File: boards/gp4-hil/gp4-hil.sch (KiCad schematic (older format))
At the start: 8 parts

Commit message: Fixed a few pinout issues. Finished full-design pinout review.
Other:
- note removed: "Design review completed for PSU+Ethernet+FPGA support"
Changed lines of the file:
@@
 Wire Wire Line
 	4200 6750 3850 6750
-Text Notes 6350 6550 0    60   ~ 0
-Design review completed for PSU+Ethernet+FPGA support
 Text Label 2850 4150 0    60   ~ 0
 VPP_SHUNT_HI

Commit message: Minor refdes placement tweaks
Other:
- note added: "Bank plan\n* 14 (1V8): Boot flash, clock, Ethernet, JTAG\n* 15 (2V5): ADCs\n* 34 (variable): DUT bank 2\n* 35 (variable): DUT bank 1"
- note removed: "Bank plan\n* 14 (1V8): Boot flash, clock, Ethernet, JTAG\n* 15 (2V5): ADCs\n* 34 (variable): DUT bank 1\n* 35 (variable): DUT bank 2"
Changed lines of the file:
@@
 $EndSheet
 Text Notes 1250 12350 0    60   ~ 0
-Bank plan\n* 14 (1V8): Boot flash, clock, Ethernet, JTAG\n* 15 (2V5): ADCs\n* 34 (variable): DUT bank 1\n* 35 (variable): DUT bank 2
+Bank plan\n* 14 (1V8): Boot flash, clock, Ethernet, JTAG\n* 15 (2V5): ADCs\n* 34 (variable): DUT bank 2\n* 35 (variable): DUT bank 1
 Text Notes 1250 11600 0    60   ~ 0
 Possibly the most overkill dev board ever.\n* Target device has 26 LUTs and 12 FFs\n* Support FPGA has 63,400 LUTs and 126800 FFs (if you load the 100t)\n* Has an ADC, DAC, and digital I/O on every pin of the DUT, all bridged out to TCP sockets\n* TCP programming, simply netcat a bitstream to the board to flash the DUT

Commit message: Added pullups to default DUT_VDDx to 1V8 instead of floating
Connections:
- net 1V8: now also R172.1, R175.1
- net GND: no longer R172.1, R175.1

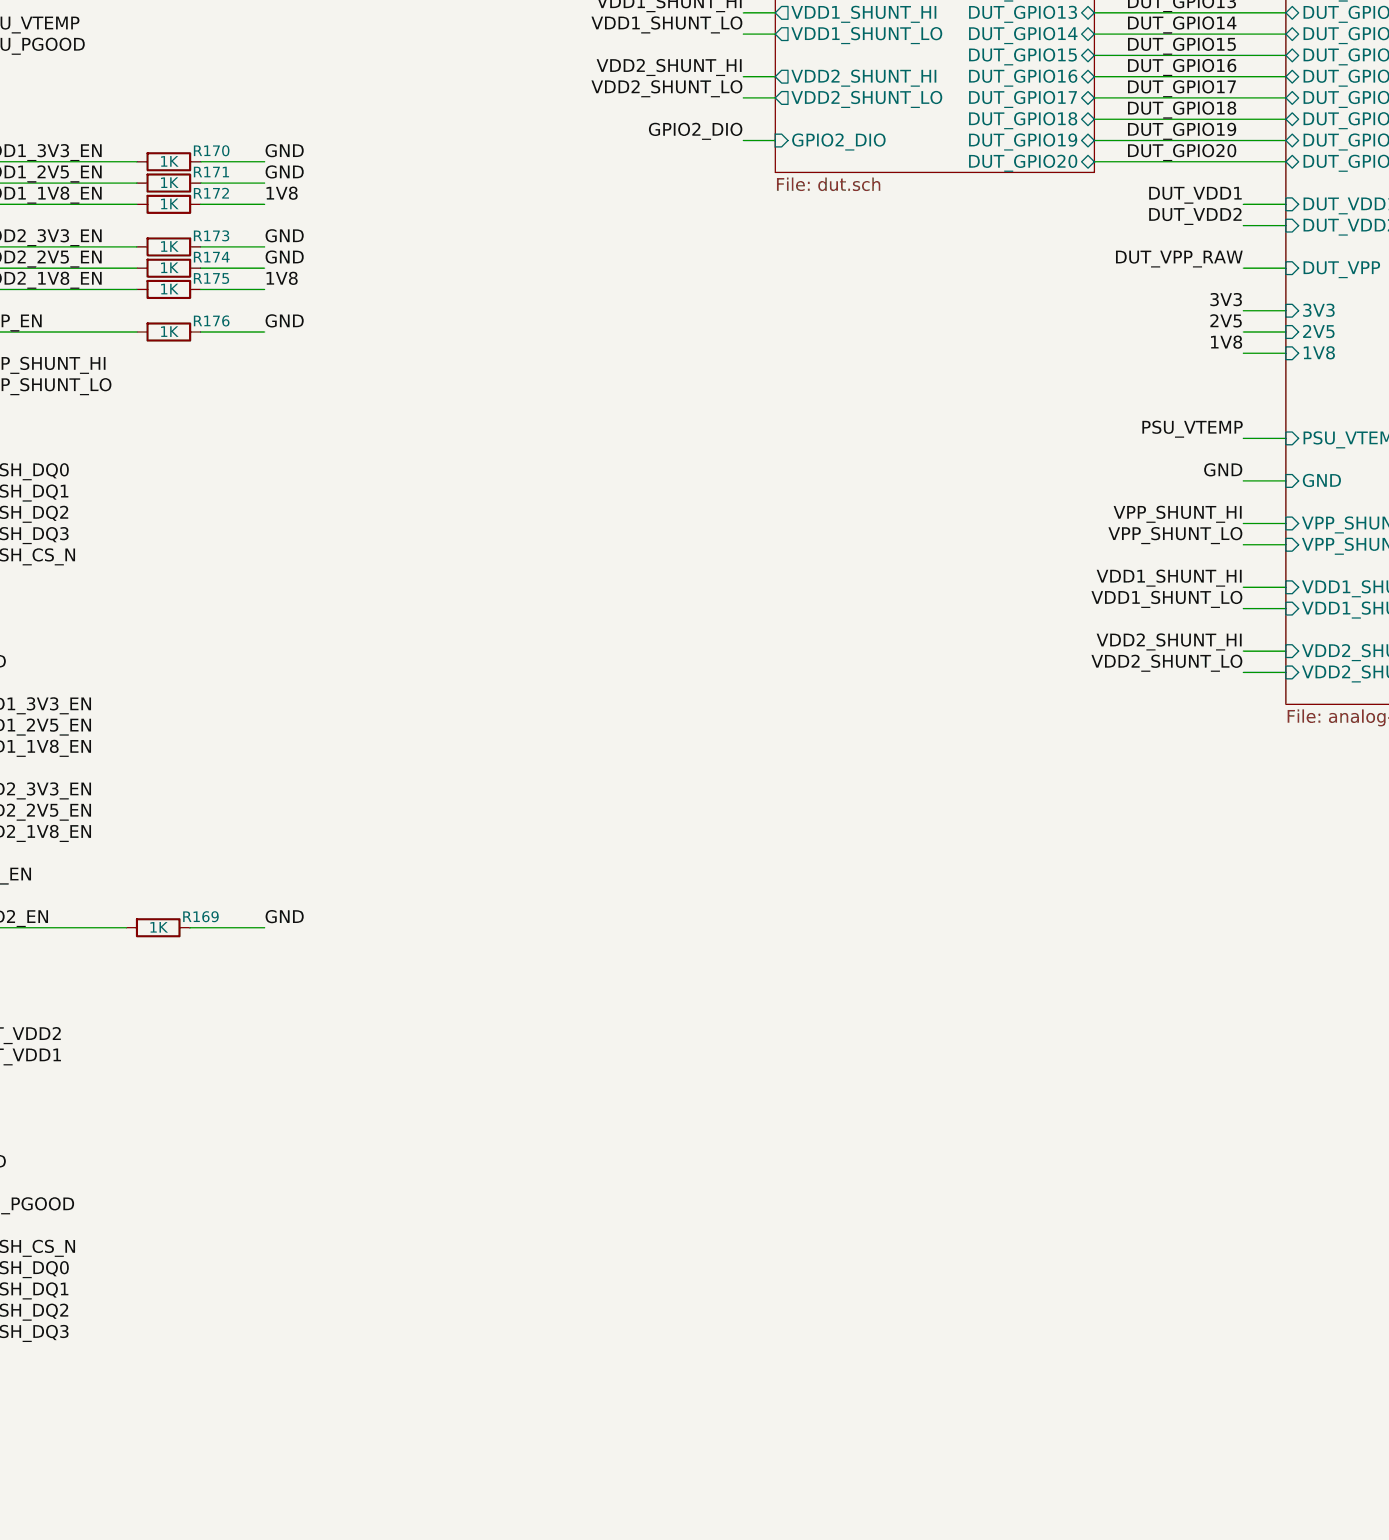
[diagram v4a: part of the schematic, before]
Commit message: Added jumpers to Vdd enable lines so they can be strapped high without FPGA involvement
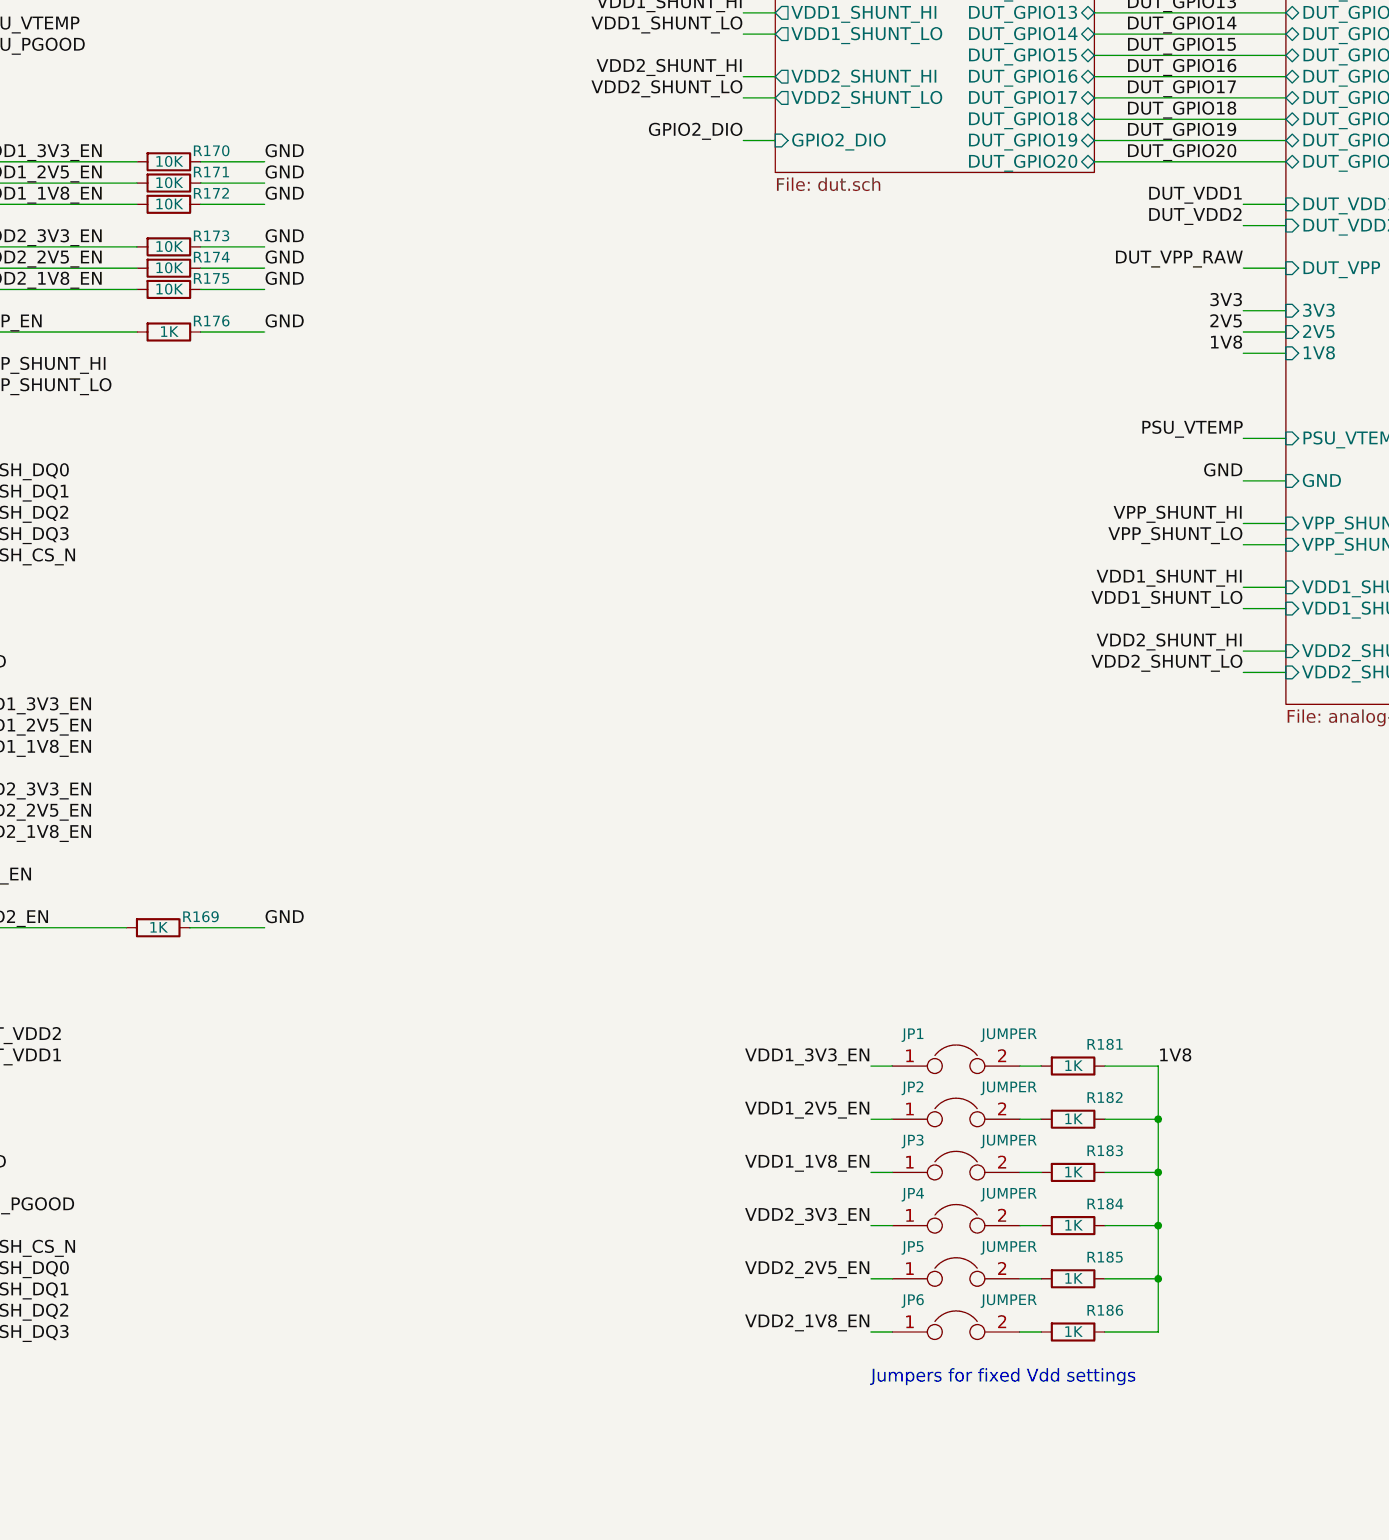
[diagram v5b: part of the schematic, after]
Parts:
- added JP1, JP2, JP3, JP4, JP5, JP6: JUMPER, symbol JUMPER
- added R181, R182, R183, R184, R185, R186: 1K, symbol R
- R170, R171, R172, R173, R174, R175: value 1K -> 10K
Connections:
- net 1V8: now also R181.1, R182.1, R183.1, R184.1, R185.1, R186.1; no longer R172.1, R175.1
- net GND: now also R172.1, R175.1
- net VDD1_1V8_EN: now also JP3.1
- net VDD1_2V5_EN: now also JP2.1
- net VDD1_3V3_EN: now also JP1.1
- net VDD2_1V8_EN: now also JP6.1
- net VDD2_2V5_EN: now also JP5.1
- net VDD2_3V3_EN: now also JP4.1
- new net: JP1.2, R181.2
- new net: JP2.2, R182.2
- new net: JP3.2, R183.2
- new net: JP4.2, R184.2
- new net: JP5.2, R185.2
- new net: JP6.2, R186.2
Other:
- note added: "Jumpers for fixed Vdd settings"
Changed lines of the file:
@@
 P 3750 3150
 F 0 "R170" V 3700 3350 50  0000 C CNN
-F 1 "1K" V 3750 3150 50  0000 C CNN
+F 1 "10K" V 3750 3150 50  0000 C CNN
 F 2 "" V 3680 3150 30  0000 C CNN
 F 3 "" H 3750 3150 30  0000 C CNN
@@
 P 3750 3250
 F 0 "R171" V 3700 3450 50  0000 C CNN
-F 1 "1K" V 3750 3250 50  0000 C CNN
+F 1 "10K" V 3750 3250 50  0000 C CNN
 F 2 "" V 3680 3250 30  0000 C CNN
 F 3 "" H 3750 3250 30  0000 C CNN
@@
 P 3750 3350
 F 0 "R172" V 3700 3550 50  0000 C CNN
-F 1 "1K" V 3750 3350 50  0000 C CNN
+F 1 "10K" V 3750 3350 50  0000 C CNN
 F 2 "" V 3680 3350 30  0000 C CNN
 F 3 "" H 3750 3350 30  0000 C CNN
@@
 P 3750 3550
 F 0 "R173" V 3700 3750 50  0000 C CNN
-F 1 "1K" V 3750 3550 50  0000 C CNN
+F 1 "10K" V 3750 3550 50  0000 C CNN
 F 2 "" V 3680 3550 30  0000 C CNN
 F 3 "" H 3750 3550 30  0000 C CNN
@@
 P 3750 3650
 F 0 "R174" V 3700 3850 50  0000 C CNN
-F 1 "1K" V 3750 3650 50  0000 C CNN
+F 1 "10K" V 3750 3650 50  0000 C CNN
 F 2 "" V 3680 3650 30  0000 C CNN
 F 3 "" H 3750 3650 30  0000 C CNN
@@
 P 3750 3750
 F 0 "R175" V 3700 3950 50  0000 C CNN
-F 1 "1K" V 3750 3750 50  0000 C CNN
+F 1 "10K" V 3750 3750 50  0000 C CNN
 F 2 "" V 3680 3750 30  0000 C CNN
 F 3 "" H 3750 3750 30  0000 C CNN
@@
 Text Label 4200 3250 0    60   ~ 0
 GND
+Text Label 4200 3650 0    60   ~ 0
+GND
+Text Label 4200 3550 0    60   ~ 0
+GND
+Text Label 4200 3950 0    60   ~ 0
+GND
+Text Label 4200 3750 0    60   ~ 0
+GND
 Text Label 4200 3350 0    60   ~ 0
+GND
+$Comp
+L JUMPER JP1
+U 1 1 577157DD
+P 7450 7400
+F 0 "JP1" H 7250 7550 50  0000 C CNN
+F 1 "JUMPER" H 7700 7550 50  0000 C CNN
+F 2 "" H 7450 7400 60  0000 C CNN
+F 3 "" H 7450 7400 60  0000 C CNN
+	1    7450 7400
+	1    0    0    -1
+$EndComp
+Text Label 7050 7400 2    60   ~ 0
+VDD1_3V3_EN
+Text Label 7050 7650 2    60   ~ 0
+VDD1_2V5_EN
+Text Label 7050 7900 2    60   ~ 0
+VDD1_1V8_EN
+Text Label 7050 8150 2    60   ~ 0
+VDD2_3V3_EN
+Text Label 7050 8400 2    60   ~ 0
+VDD2_2V5_EN
+Text Label 7050 8650 2    60   ~ 0
+VDD2_1V8_EN
+Text Notes 7050 8900 0    60   ~ 0
+Jumpers for fixed Vdd settings
+Text Label 8400 7400 0    60   ~ 0
 1V8
-Text Label 4200 3750 0    60   ~ 0
-1V8
-Text Label 4200 3650 0    60   ~ 0
-GND
-Text Label 4200 3550 0    60   ~ 0
-GND
-Text Label 4200 3950 0    60   ~ 0
-GND
+$Comp
+L JUMPER JP2
+U 1 1 5771B47A
+P 7450 7650
+F 0 "JP2" H 7250 7800 50  0000 C CNN
+F 1 "JUMPER" H 7700 7800 50  0000 C CNN
+F 2 "" H 7450 7650 60  0000 C CNN
+F 3 "" H 7450 7650 60  0000 C CNN
+	1    7450 7650
+	1    0    0    -1
+$EndComp
+$Comp
+L JUMPER JP3
+U 1 1 5771B86E
+P 7450 7900
+F 0 "JP3" H 7250 8050 50  0000 C CNN
+F 1 "JUMPER" H 7700 8050 50  0000 C CNN
+F 2 "" H 7450 7900 60  0000 C CNN
+F 3 "" H 7450 7900 60  0000 C CNN
+	1    7450 7900
+	1    0    0    -1
+$EndComp
+$Comp
+L JUMPER JP4
+U 1 1 5771C029
+P 7450 8150
+F 0 "JP4" H 7250 8300 50  0000 C CNN
+F 1 "JUMPER" H 7700 8300 50  0000 C CNN
+F 2 "" H 7450 8150 60  0000 C CNN
+F 3 "" H 7450 8150 60  0000 C CNN
+	1    7450 8150
+	1    0    0    -1
+$EndComp
+$Comp
+L JUMPER JP5
+U 1 1 5771C419
+P 7450 8400
+F 0 "JP5" H 7250 8550 50  0000 C CNN
+F 1 "JUMPER" H 7700 8550 50  0000 C CNN
+F 2 "" H 7450 8400 60  0000 C CNN
+F 3 "" H 7450 8400 60  0000 C CNN
+	1    7450 8400
+	1    0    0    -1
+$EndComp
+$Comp
+L JUMPER JP6
+U 1 1 5771C80E
+P 7450 8650
+F 0 "JP6" H 7250 8800 50  0000 C CNN
+F 1 "JUMPER" H 7700 8800 50  0000 C CNN
+F 2 "" H 7450 8650 60  0000 C CNN
+F 3 "" H 7450 8650 60  0000 C CNN
+	1    7450 8650
+	1    0    0    -1
+$EndComp
+Wire Wire Line
+	8150 7400 8400 7400
+Wire Wire Line
+	8400 8650 8400 7400
+Wire Wire Line
+	8150 8650 8400 8650
+Wire Wire Line
+	8150 8400 8400 8400
+Connection ~ 8400 8400
+Wire Wire Line
+	8150 8150 8400 8150
+Connection ~ 8400 8150
+Wire Wire Line
+	8150 7900 8400 7900
+Connection ~ 8400 7900
+Wire Wire Line
+	8150 7650 8400 7650
+Connection ~ 8400 7650
+Wire Wire Line
+	7150 7400 7050 7400
+Wire Wire Line
+	7050 7650 7150 7650
+Wire Wire Line
+	7150 7900 7050 7900
+Wire Wire Line
+	7050 8150 7150 8150
+Wire Wire Line
+	7150 8400 7050 8400
+Wire Wire Line
+	7050 8650 7150 8650
+$Comp
+L R R181
+U 1 1 57721AE1
+P 8000 7400
+F 0 "R181" V 7900 7550 50  0000 C CNN
+F 1 "1K" V 8000 7400 50  0000 C CNN
+F 2 "" V 7930 7400 30  0000 C CNN
+F 3 "" H 8000 7400 30  0000 C CNN
+	1    8000 7400
+	0    1    1    0
+$EndComp
+$Comp
+L R R182
+U 1 1 57727DC9
+P 8000 7650
+F 0 "R182" V 7900 7800 50  0000 C CNN
+F 1 "1K" V 8000 7650 50  0000 C CNN
+F 2 "" V 7930 7650 30  0000 C CNN
+F 3 "" H 8000 7650 30  0000 C CNN
+	1    8000 7650
+	0    1    1    0
+$EndComp
+$Comp
+L R R183
+U 1 1 577283B9
+P 8000 7900
+F 0 "R183" V 7900 8050 50  0000 C CNN
+F 1 "1K" V 8000 7900 50  0000 C CNN
+F 2 "" V 7930 7900 30  0000 C CNN
+F 3 "" H 8000 7900 30  0000 C CNN
+	1    8000 7900
+	0    1    1    0
+$EndComp
+$Comp
+L R R184
+U 1 1 577289B1
+P 8000 8150
+F 0 "R184" V 7900 8300 50  0000 C CNN
+F 1 "1K" V 8000 8150 50  0000 C CNN
+F 2 "" V 7930 8150 30  0000 C CNN
+F 3 "" H 8000 8150 30  0000 C CNN
+	1    8000 8150
+	0    1    1    0
+$EndComp
+$Comp
+L R R185
+U 1 1 57728F9D
+P 8000 8400
+F 0 "R185" V 7900 8550 50  0000 C CNN
+F 1 "1K" V 8000 8400 50  0000 C CNN
+F 2 "" V 7930 8400 30  0000 C CNN
+F 3 "" H 8000 8400 30  0000 C CNN
+	1    8000 8400
+	0    1    1    0
+$EndComp
+$Comp
+L R R186
+U 1 1 57729595
+P 8000 8650
+F 0 "R186" V 7900 8800 50  0000 C CNN
+F 1 "1K" V 8000 8650 50  0000 C CNN
+F 2 "" V 7930 8650 30  0000 C CNN
+F 3 "" H 8000 8650 30  0000 C CNN
+	1    8000 8650
+	0    1    1    0
+$EndComp
+Wire Wire Line
+	7750 8650 7850 8650
+Wire Wire Line
+	7850 8400 7750 8400
+Wire Wire Line
+	7750 8150 7850 8150
+Wire Wire Line
+	7850 7900 7750 7900
+Wire Wire Line
+	7750 7650 7850 7650
+Wire Wire Line
+	7750 7400 7850 7400
 $EndSCHEMATC

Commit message: Added pi filter to A2V5_ETH for isolation from digital noise
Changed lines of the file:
@@
 	8150 7400 8400 7400
 Wire Wire Line
-	8400 8650 8400 7400
+	8400 7400 8400 8650
 Wire Wire Line
-	8150 8650 8400 8650
+	8400 8650 8150 8650
 Wire Wire Line
 	8150 8400 8400 8400

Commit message: Added some extra ground points for probing
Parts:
- added TP34, TP35, TP36: TESTPOINT, symbol CONN_01X01
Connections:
- net GND: now also TP34.1 (P1), TP35.1 (P1), TP36.1 (P1)
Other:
- note added: "Extra ground clips"
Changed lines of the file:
@@
 Wire Wire Line
 	7750 7400 7850 7400
+Text Notes 9900 8900 0    60   ~ 0
+Extra ground clips
+$Comp
+L CONN_01X01 TP36
+U 1 1 57760681
+P 9950 8650
+F 0 "TP36" H 10100 8650 50  0000 C CNN
+F 1 "TESTPOINT" H 9600 8600 50  0000 C CNN
+F 2 "" H 9950 8650 60  0000 C CNN
+F 3 "" H 9950 8650 60  0000 C CNN
+	1    9950 8650
+	-1   0    0    1
+$EndComp
+Text Label 10650 8650 0    60   ~ 0
+GND
+$Comp
+L CONN_01X01 TP35
+U 1 1 57762E44
+P 9950 8400
+F 0 "TP35" H 10100 8400 50  0000 C CNN
+F 1 "TESTPOINT" H 9600 8350 50  0000 C CNN
+F 2 "" H 9950 8400 60  0000 C CNN
+F 3 "" H 9950 8400 60  0000 C CNN
+	1    9950 8400
+	-1   0    0    1
+$EndComp
+$Comp
+L CONN_01X01 TP34
+U 1 1 57763254
+P 9950 8150
+F 0 "TP34" H 10100 8150 50  0000 C CNN
+F 1 "TESTPOINT" H 9600 8100 50  0000 C CNN
+F 2 "" H 9950 8150 60  0000 C CNN
+F 3 "" H 9950 8150 60  0000 C CNN
+	1    9950 8150
+	-1   0    0    1
+$EndComp
+Wire Wire Line
+	10150 8150 10650 8150
+Wire Wire Line
+	10650 8150 10650 8650
+Wire Wire Line
+	10150 8400 10650 8400
+Connection ~ 10650 8400
+Wire Wire Line
+	10650 8650 10150 8650
 $EndSCHEMATC
